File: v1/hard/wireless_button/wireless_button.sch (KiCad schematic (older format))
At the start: 21 parts, among them J1 USB_B_Micro, J2 RJ12, J3 Conn_01x01_Female, Q1 Q_PMOS_GSD, SW1 SW_Push, U1 STM32F103C8Tx, U2 CC1101_MOD, U3 OLED_0.91

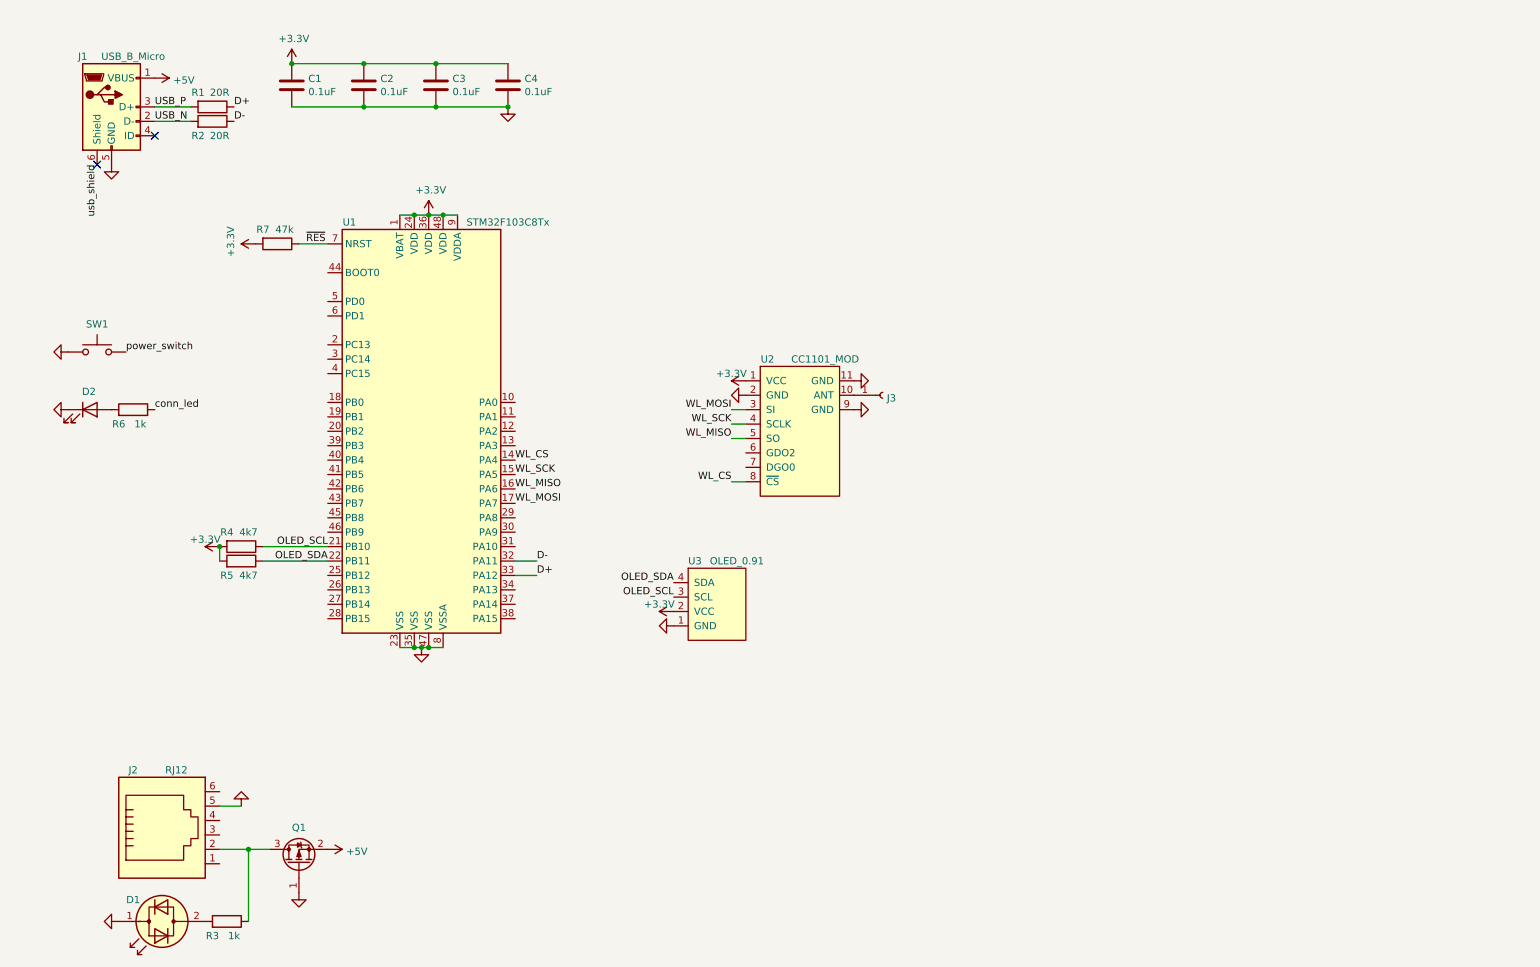
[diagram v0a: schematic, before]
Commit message: Wireless button PCB updates. - added EEPROM - added connector for "pull-up" opto output - added overvoltage protection zener between source and gate of reverse protecting MOSFETs
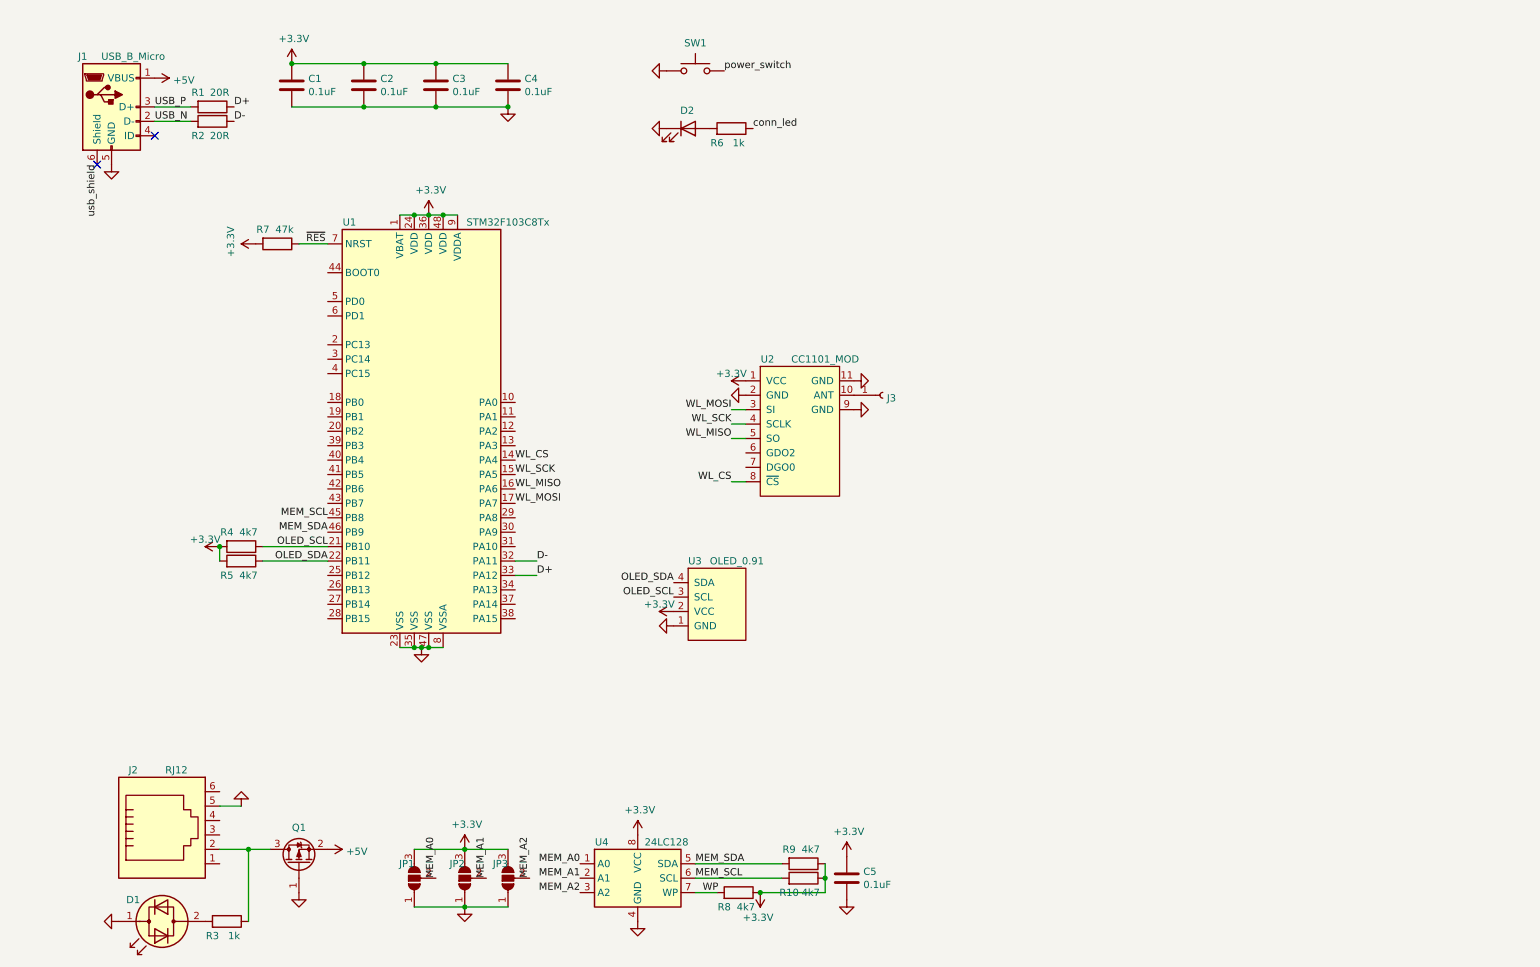
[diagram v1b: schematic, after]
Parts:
- added C5: 0.1uF, Resistor_SMD:R_0805_2012Metric_Pad1.15x1.40mm_HandSolder, symbol Device:C
- added JP1: A0, Jumper:SolderJumper-3_P2.0mm_Open_TrianglePad1.0x1.5mm, symbol Jumper:SolderJumper_3_Open
- added JP2: A1, Jumper:SolderJumper-3_P2.0mm_Open_TrianglePad1.0x1.5mm, symbol Jumper:SolderJumper_3_Open
- added JP3: A2, Jumper:SolderJumper-3_P2.0mm_Open_TrianglePad1.0x1.5mm, symbol Jumper:SolderJumper_3_Open
- added R10, R8, R9: 4k7, Resistor_SMD:R_0805_2012Metric_Pad1.15x1.40mm_HandSolder, symbol Device:R
- added U4: 24LC128, Package_SO:TSSOP-8_4.4x3mm_P0.65mm, symbol Memory_EEPROM:24LC128
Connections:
- net +3V3: now also C5.1, JP1.3 (B), JP2.3 (B), JP3.3 (B), R10.1, R8.1, R9.1, U4.8 (VCC)
- net GND: now also C5.2, JP1.1 (A), JP2.1 (A), JP3.1 (A), U4.4 (GND)
- net MEM_SCL: now reaches U1.45 (PB8)
- net MEM_SCL: now also R10.2, U4.6 (SCL)
- net MEM_SDA: now reaches U1.46 (PB9)
- net MEM_SDA: now also R9.2, U4.5 (SDA)
- new net MEM_A0: JP1.2 (C), U4.1 (A0)
- new net MEM_A1: JP2.2 (C), U4.2 (A1)
- new net MEM_A2: JP3.2 (C), U4.3 (A2)
- new net WP: R8.2, U4.7 (WP)
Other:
- moved on the sheet: D2, R6, SW1

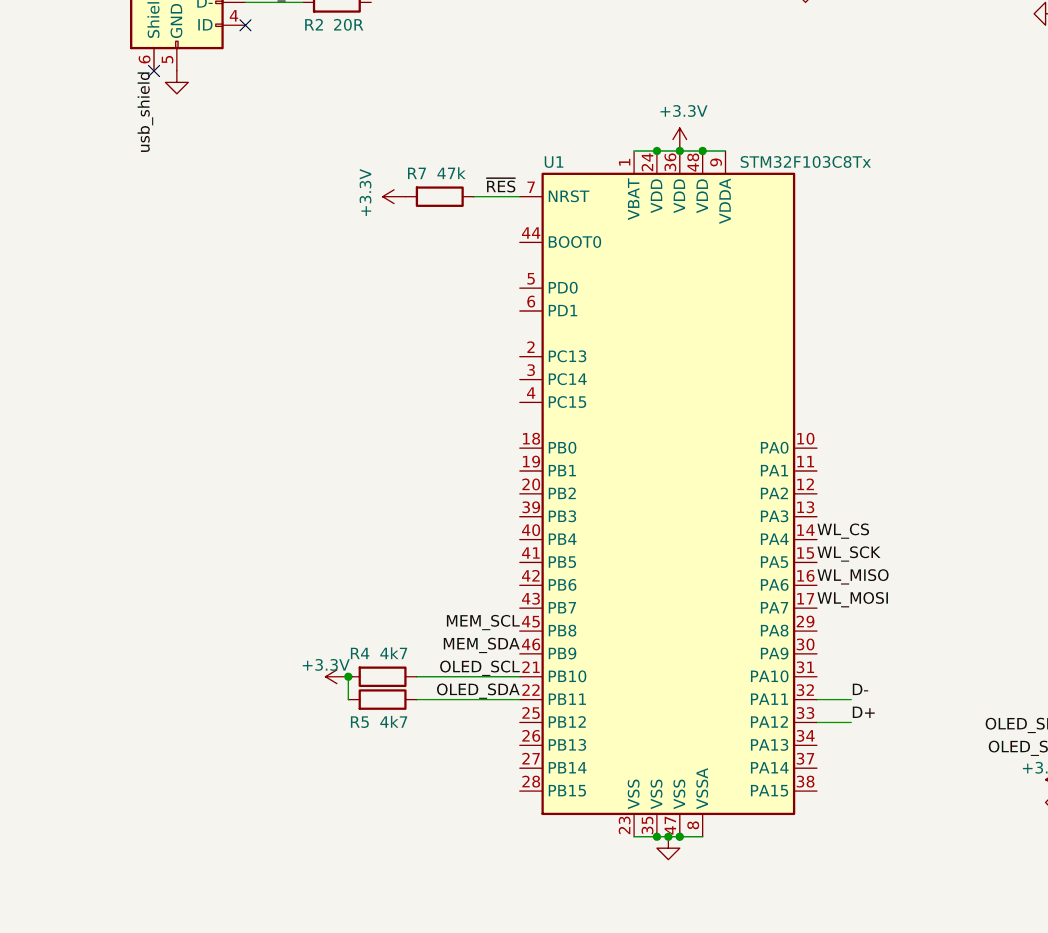
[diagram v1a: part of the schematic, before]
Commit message: !!! Important. This is last commit before changing case from 1593L (aka BMD 60035) to G01B. !!! Many additions to wireless button. Came to conclusion that box is too small, mostly because of cuts on board sides. Also desided to drop idea powering from Li-batteriies and change to non rechangable +9V.
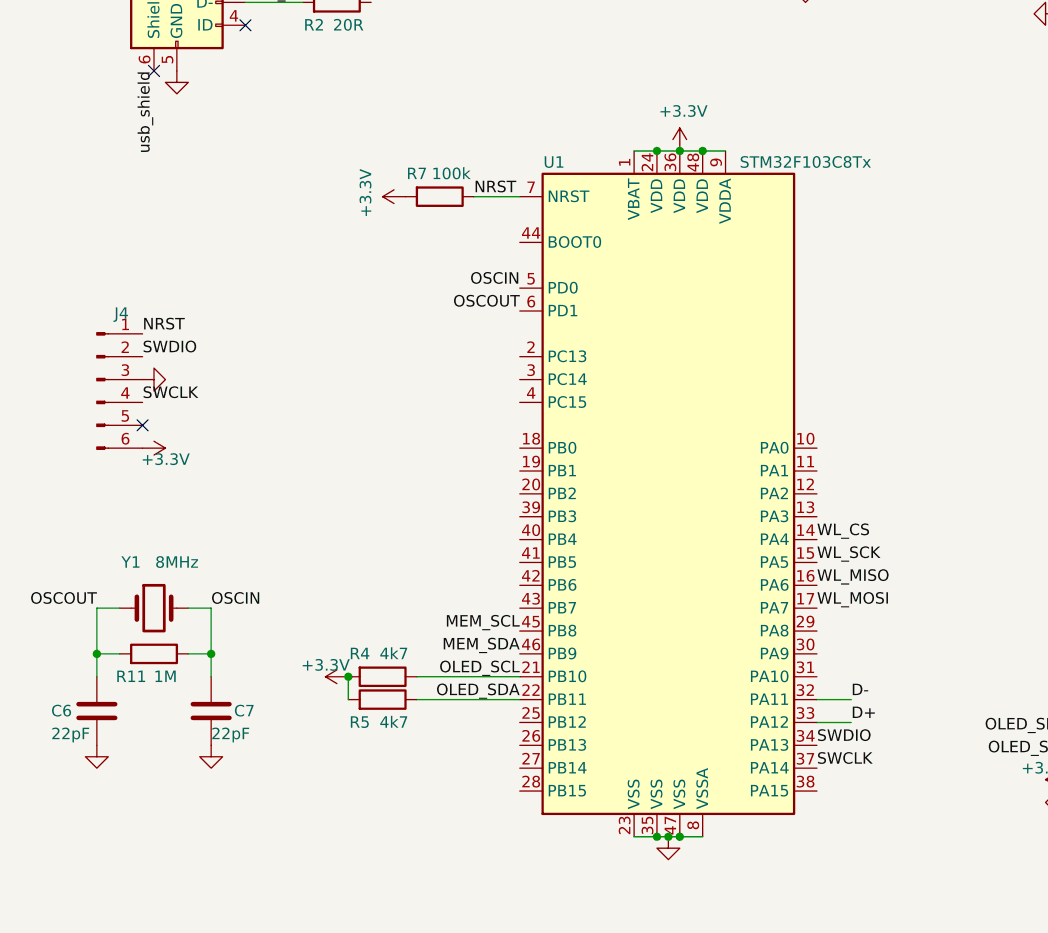
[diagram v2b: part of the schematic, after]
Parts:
- added C6, C7: 22pF, Resistor_SMD:R_0805_2012Metric_Pad1.15x1.40mm_HandSolder, symbol Device:C
- added J4: Conn_01x06_Male, Connector_PinSocket_2.54mm:PinSocket_1x06_P2.54mm_Vertical, symbol Connector:Conn_01x06_Male
- added R11: 1M, Resistor_SMD:R_1206_3216Metric_Pad1.42x1.75mm_HandSolder, symbol Device:R
- added Y1: 8MHz, Crystal:Crystal_SMD_5032-2Pin_5.0x3.2mm, symbol Device:Crystal
- R7: value 47k -> 100k
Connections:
- net +3V3: now also J4.6 (Pin_6)
- net GND: now also C6.2, C7.2, J4.3 (Pin_3)
- net SWDIO: now reaches U1.34 (PA13)
- net SWDIO: now also J4.2 (Pin_2)
- net SWCLK: now reaches U1.37 (PA14)
- net SWCLK: now also J4.4 (Pin_4)
- net OSCIN: now reaches U1.5 (PD0)
- net OSCIN: now also C7.1, R11.1, Y1.2
- net OSCOUT: now reaches U1.6 (PD1)
- net OSCOUT: now also C6.1, R11.2, Y1.1
- net ~RES renamed NRST
- net NRST: now also J4.1 (Pin_1)
- no-connect marks 2 -> 3
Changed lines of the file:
@@
-	1    0    0    -1
-$EndComp
-$Comp
-L power:GND #PWR0102
-U 1 1 607A51E3
-P 3400 5050
-F 0 "#PWR0102" H 3400 4800 50  0001 C CNN
-F 1 "GND" H 3405 4877 50  0001 C CNN
-F 2 "" H 3400 5050 50  0001 C CNN
-F 3 "" H 3400 5050 50  0001 C CNN
-	1    3400 5050
 	1    0    0    -1
 $EndComp
@@
 P 2400 2250
 F 0 "R7" V 2300 2150 50  0000 C CNN
-F 1 "47k" V 2300 2300 50  0000 C CNN
+F 1 "100k" V 2300 2300 50  0000 C CNN
 F 2 "Resistor_SMD:R_0805_2012Metric_Pad1.15x1.40mm_HandSolder" V 2330 2250 50  0001 C CNN
 F 3 "~" H 2400 2250 50  0001 C CNN
@@
 Wire Wire Line
 	2550 2250 2750 2250
-Text Label 2600 2250 0    50   ~ 0
-~RES
 $Comp
 L power:+3.3V #PWR0120
@@
 Text Label 4150 6650 1    50   ~ 0
 MEM_A2
+$Comp
+L Connector:Conn_01x06_Male J4
+U 1 1 6086294F
+P 900 3050
+F 0 "J4" H 1008 3339 50  0000 C CNN
+F 1 "Conn_01x06_Male" H 1008 3340 50  0001 C CNN
+F 2 "Connector_PinSocket_2.54mm:PinSocket_1x06_P2.54mm_Vertical" H 900 3050 50  0001 C CNN
+F 3 "~" H 900 3050 50  0001 C CNN
+	1    900  3050
+	1    0    0    -1
+$EndComp
+Text Label 1100 2850 0    50   ~ 0
+NRST
+Text Label 1100 2950 0    50   ~ 0
+SWDIO
+Text Label 1100 3150 0    50   ~ 0
+SWCLK
+$Comp
+L power:GND #PWR0128
+U 1 1 60865389
+P 1100 3050
+F 0 "#PWR0128" H 1100 2800 50  0001 C CNN
+F 1 "GND" H 1105 2877 50  0001 C CNN
+F 2 "" H 1100 3050 50  0001 C CNN
+F 3 "" H 1100 3050 50  0001 C CNN
+	1    1100 3050
+	0    -1   -1   0
+$EndComp
+NoConn ~ 1100 3250
+$Comp
+L power:+3.3V #PWR0129
+U 1 1 60866D48
+P 1100 3350
+F 0 "#PWR0129" H 1100 3200 50  0001 C CNN
+F 1 "+3.3V" V 1150 3450 50  0000 C CNN
+F 2 "" H 1100 3350 50  0001 C CNN
+F 3 "" H 1100 3350 50  0001 C CNN
+	1    1100 3350
+	0    1    1    0
+$EndComp
+Text Label 2550 2250 0    50   ~ 0
+NRST
+Text Label 4050 4750 0    50   ~ 0
+SWCLK
+Text Label 4050 4650 0    50   ~ 0
+SWDIO
+$Comp
+L Device:Crystal Y1
+U 1 1 60875389
+P 1150 4050
+F 0 "Y1" H 1050 4250 50  0000 C CNN
+F 1 "8MHz" H 1250 4250 50  0000 C CNN
+F 2 "Crystal:Crystal_SMD_5032-2Pin_5.0x3.2mm" H 1150 4050 50  0001 C CNN
+F 3 "~" H 1150 4050 50  0001 C CNN
+	1    1150 4050
+	1    0    0    -1
+$EndComp
+$Comp
+L Device:C C6
+U 1 1 60875D4F
+P 900 4500
+F 0 "C6" H 700 4500 50  0000 L CNN
+F 1 "22pF" H 700 4400 50  0000 L CNN
+F 2 "Resistor_SMD:R_0805_2012Metric_Pad1.15x1.40mm_HandSolder" H 938 4350 50  0001 C CNN
+F 3 "~" H 900 4500 50  0001 C CNN
+	1    900  4500
+	1    0    0    -1
+$EndComp
+$Comp
+L Device:C C7
+U 1 1 60876493
+P 1400 4500
+F 0 "C7" H 1500 4500 50  0000 L CNN
+F 1 "22pF" H 1400 4400 50  0000 L CNN
+F 2 "Resistor_SMD:R_0805_2012Metric_Pad1.15x1.40mm_HandSolder" H 1438 4350 50  0001 C CNN
+F 3 "~" H 1400 4500 50  0001 C CNN
+	1    1400 4500
+	1    0    0    -1
+$EndComp
+Wire Wire Line
+	1300 4050 1400 4050
+Wire Wire Line
+	1400 4050 1400 4250
+Wire Wire Line
+	1000 4050 900  4050
+Wire Wire Line
+	900  4050 900  4250
+Text Label 1400 4050 0    50   ~ 0
+OSCIN
+Text Label 900  4050 2    50   ~ 0
+OSCOUT
+$Comp
+L power:GND #PWR0102
+U 1 1 607A51E3
+P 3400 5050
+F 0 "#PWR0102" H 3400 4800 50  0001 C CNN
+F 1 "GND" H 3405 4877 50  0001 C CNN
+F 2 "" H 3400 5050 50  0001 C CNN
+F 3 "" H 3400 5050 50  0001 C CNN
+	1    3400 5050
+	1    0    0    -1
+$EndComp
+$Comp
+L power:GND #PWR0130
+U 1 1 6087D0C8
+P 1400 4650
+F 0 "#PWR0130" H 1400 4400 50  0001 C CNN
+F 1 "GND" H 1405 4477 50  0001 C CNN
+F 2 "" H 1400 4650 50  0001 C CNN
+F 3 "" H 1400 4650 50  0001 C CNN
+	1    1400 4650
+	1    0    0    -1
+$EndComp
+$Comp
+L power:GND #PWR0131
+U 1 1 6087D5C3
+P 900 4650
+F 0 "#PWR0131" H 900 4400 50  0001 C CNN
+F 1 "GND" H 905 4477 50  0001 C CNN
+F 2 "" H 900 4650 50  0001 C CNN
+F 3 "" H 900 4650 50  0001 C CNN
+	1    900  4650
+	1    0    0    -1
+$EndComp
+Text Label 2750 2650 2    50   ~ 0
+OSCIN
+Text Label 2750 2750 2    50   ~ 0
+OSCOUT
+$Comp
+L Device:R R11
+U 1 1 6087F552
+P 1150 4250
+F 0 "R11" V 1050 4150 50  0000 C CNN
+F 1 "1M" V 1050 4300 50  0000 C CNN
+F 2 "Resistor_SMD:R_1206_3216Metric_Pad1.42x1.75mm_HandSolder" V 1080 4250 50  0001 C CNN
+F 3 "~" H 1150 4250 50  0001 C CNN
+	1    1150 4250
+	0    1    -1   0
+$EndComp
+Wire Wire Line
+	1300 4250 1400 4250
+Connection ~ 1400 4250
+Wire Wire Line
+	1400 4250 1400 4350
+Wire Wire Line
+	1000 4250 900  4250
+Connection ~ 900  4250
+Wire Wire Line
+	900  4250 900  4350
 $EndSCHEMATC
